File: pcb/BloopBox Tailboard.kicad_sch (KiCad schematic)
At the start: 10 parts, among them J1 USB_C_Receptacle_Power, J2 Barrel_Jack, J3 Mainboard, SW1 Button2, SW2 Button1, U1 HT7533-1

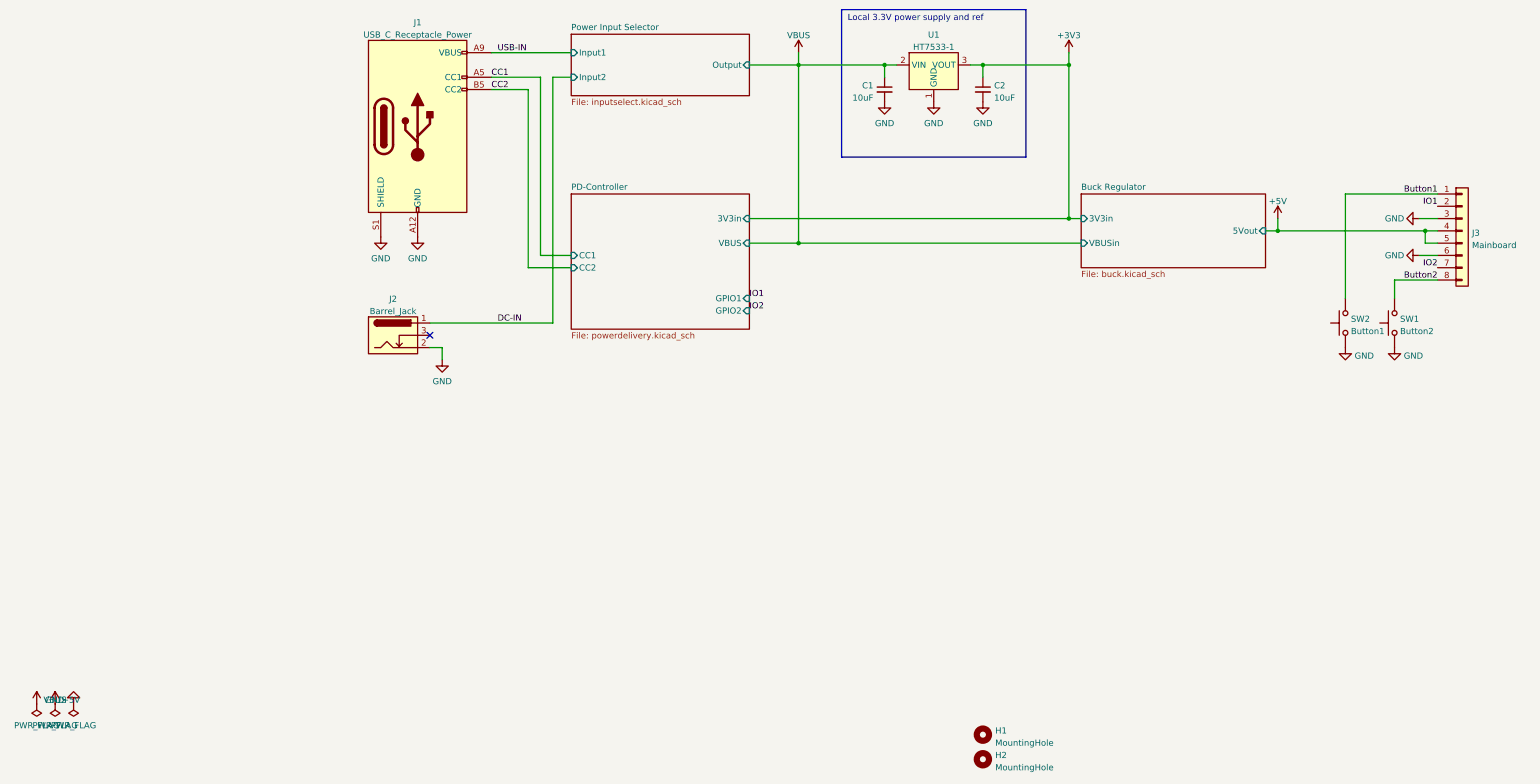
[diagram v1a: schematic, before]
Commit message: fix!: remove Power Delivery circuitry
PD circuit was removed because it didn't work as planned in the current version and fixing it would make the board too expensive. The USB-C port is now hardwired to request 5V/3A.
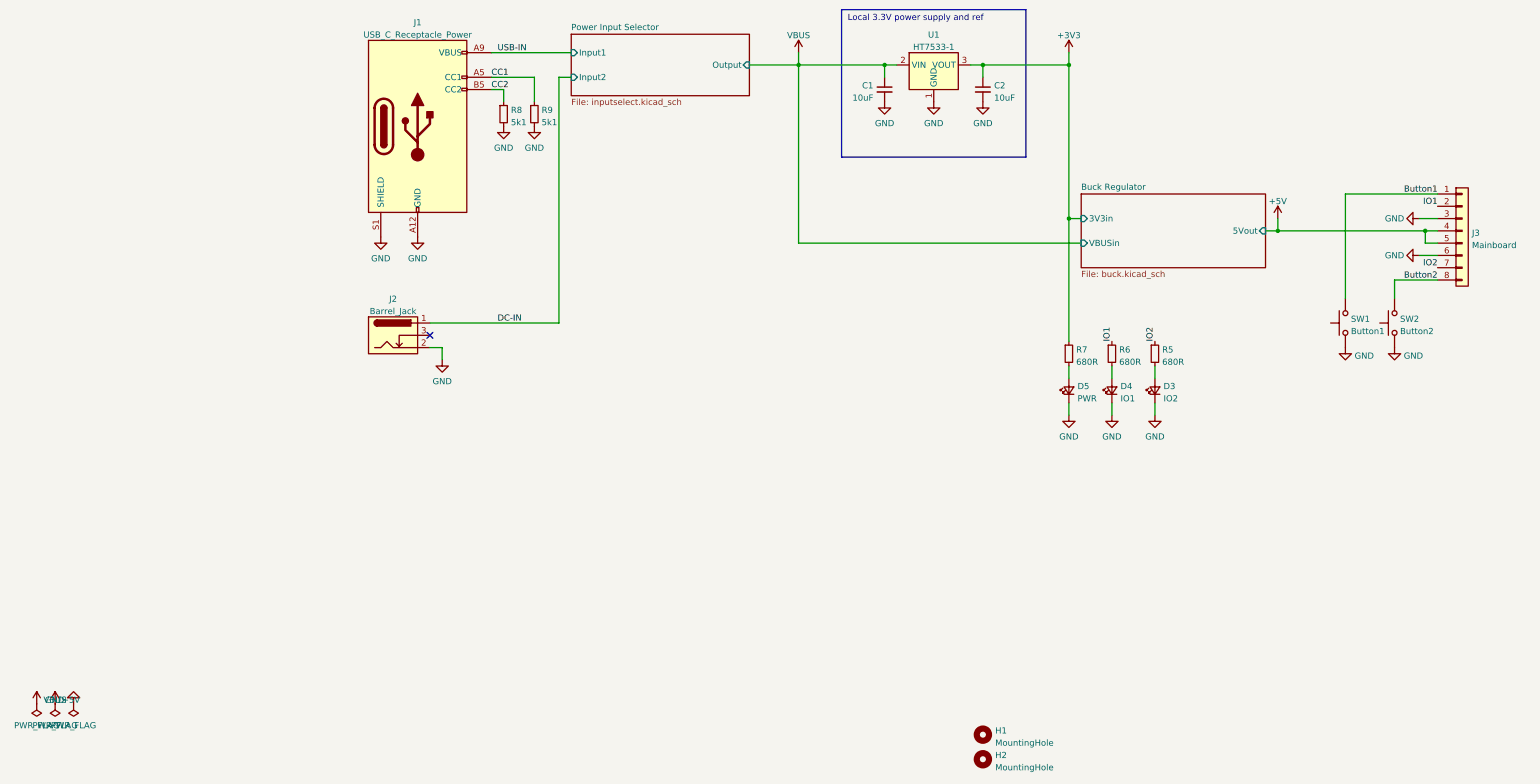
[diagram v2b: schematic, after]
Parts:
- added D3: IO2, LED_SMD:LED_0603_1608Metric, symbol Device:LED_Small
- added D4: IO1, LED_SMD:LED_0603_1608Metric, symbol Device:LED_Small
- added D5: PWR, LED_SMD:LED_0603_1608Metric, symbol Device:LED_Small
- added R5, R6, R7: 680R, Resistor_SMD:R_0402_1005Metric, symbol Device:R_Small
- added R8, R9: 5k1, Resistor_SMD:R_0402_1005Metric, symbol Device:R_Small
- renumbered SW2 to SW1, SW1 to SW2
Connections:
- net +3V3: now also R7.1
- net CC1: now also R9.1
- net CC2: now also R8.1
- net GND: now also D3.1 (K), D4.1 (K), D5.1 (K), R8.2, R9.2
- net IO1: now also R6.1
- net IO2: now also R5.1
- new net: D4.2 (A), R6.2
- new net: D3.2 (A), R5.2
- new net: D5.2 (A), R7.2
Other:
- removed sheet PD-Controller

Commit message: fix: add missing LCSC part numbers
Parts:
- R5, R6, R7: LCSC (none) -> C25130
- R8, R9: LCSC (none) -> C25905
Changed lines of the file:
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@@
       (effects (font (size 1.27 1.27)) hide)
     )
-    (property "LCSC" "" (id 4) (at 194.31 109.22 0)
+    (property "LCSC" "C25130" (id 4) (at 194.31 109.22 0)
       (effects (font (size 1.27 1.27)) hide)
     )
@@
       (effects (font (size 1.27 1.27)) hide)
     )
+    (property "LCSC" "C25905" (id 4) (at 59.69 59.69 0)
+      (effects (font (size 1.27 1.27)) hide)
+    )
     (pin "1")
     (pin "2")
@@
       (effects (font (size 1.27 1.27)) hide)
     )
-    (property "LCSC" "" (id 4) (at 176.53 109.22 0)
+    (property "LCSC" "C25130" (id 4) (at 176.53 109.22 0)
       (effects (font (size 1.27 1.27)) hide)
     )
@@
       (effects (font (size 1.27 1.27)) hide)
     )
-    (property "LCSC" "" (id 4) (at 185.42 109.22 0)
+    (property "LCSC" "C25130" (id 4) (at 185.42 109.22 0)
       (effects (font (size 1.27 1.27)) hide)
     )
@@
     )
     (property "Datasheet" "~" (id 3) (at 66.04 59.69 0)
+      (effects (font (size 1.27 1.27)) hide)
+    )
+    (property "LCSC" "C25905" (id 4) (at 66.04 59.69 0)
       (effects (font (size 1.27 1.27)) hide)
     )
@@
     )
     (path "/1b44a7b4-b5f4-46d8-99d8-93dacc546a27/b33034bf-543f-4856-be58-4644f3192a6c"
-      (reference "R16") (unit 1) (value "13k") (footprint "Resistor_SMD:R_0402_1005Metric")
+      (reference "R16") (unit 1) (value "20k") (footprint "Resistor_SMD:R_0402_1005Metric")
     )
     (path "/1b44a7b4-b5f4-46d8-99d8-93dacc546a27/1d840180-3569-4e7f-b585-580f8806e35b"
@@
     )
     (path "/1b44a7b4-b5f4-46d8-99d8-93dacc546a27/bc87f9a8-a9b9-4728-a1a0-f8aa6d17f36e"
-      (reference "R18") (unit 1) (value "22k") (footprint "Resistor_SMD:R_0402_1005Metric")
+      (reference "R18") (unit 1) (value "33k") (footprint "Resistor_SMD:R_0402_1005Metric")
     )
     (path "/8587232f-a474-4071-bc11-98a1506a86b8/9d1bcf1d-e8a1-4daa-8342-8e3f12d5c9f2"
